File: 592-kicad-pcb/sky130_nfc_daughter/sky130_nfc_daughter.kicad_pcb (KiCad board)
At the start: 4 copper layers, 50 x 52 mm, 109 parts, among them J1 U.FL-R-SMT-1_80_, J10 U.FL-R-SMT-1_80_, J2 U.FL-R-SMT-1_80_, J3 U.FL-R-SMT-1_80_, J4 U.FL-R-SMT-1_80_, J5 U.FL-R-SMT-1_80_, J6 U.FL-R-SMT-1_80_, J7 U.FL-R-SMT-1_80_, J8 DF40C-40DS-0.4V_51_, J9 DF40C-40DS-0.4V_51_, SW1 SW_Push, U1 Caravel_QFN, U3 W25Q32JVZP

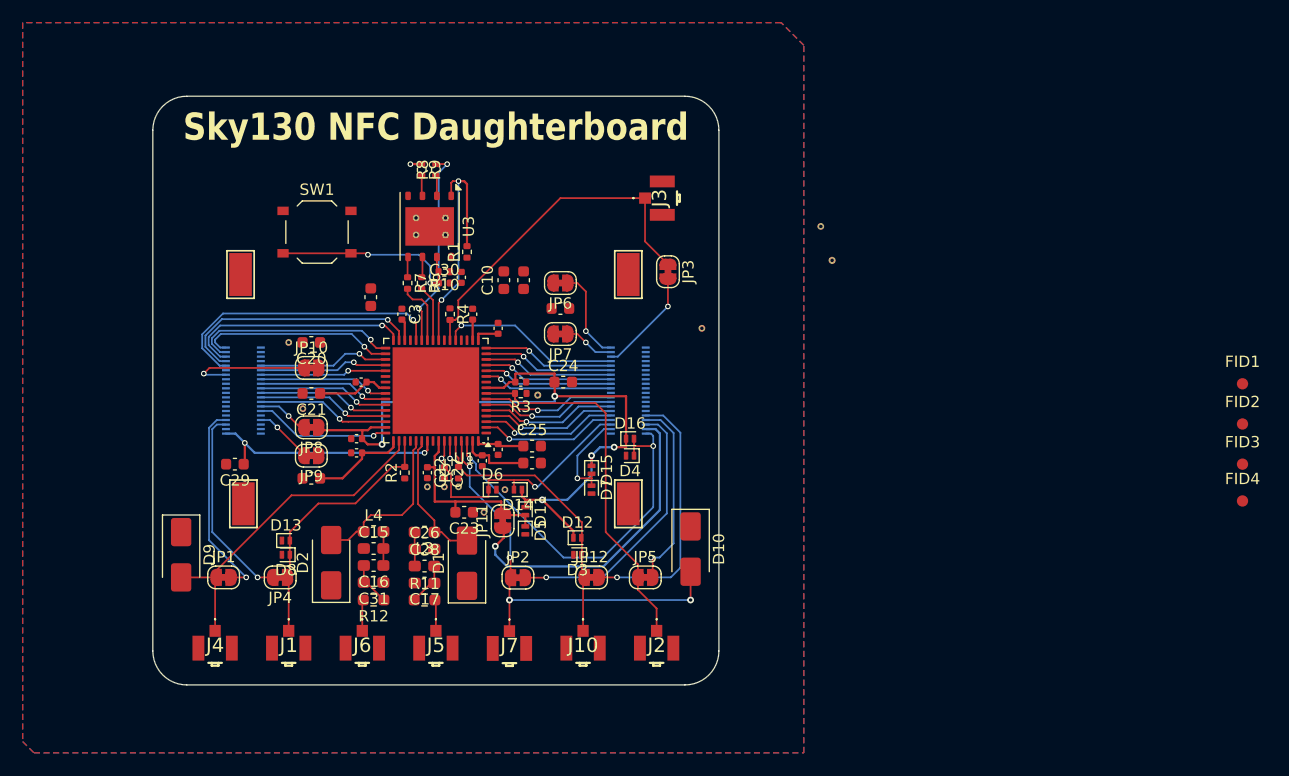
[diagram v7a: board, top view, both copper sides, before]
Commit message: daughterboard routing, 90% done
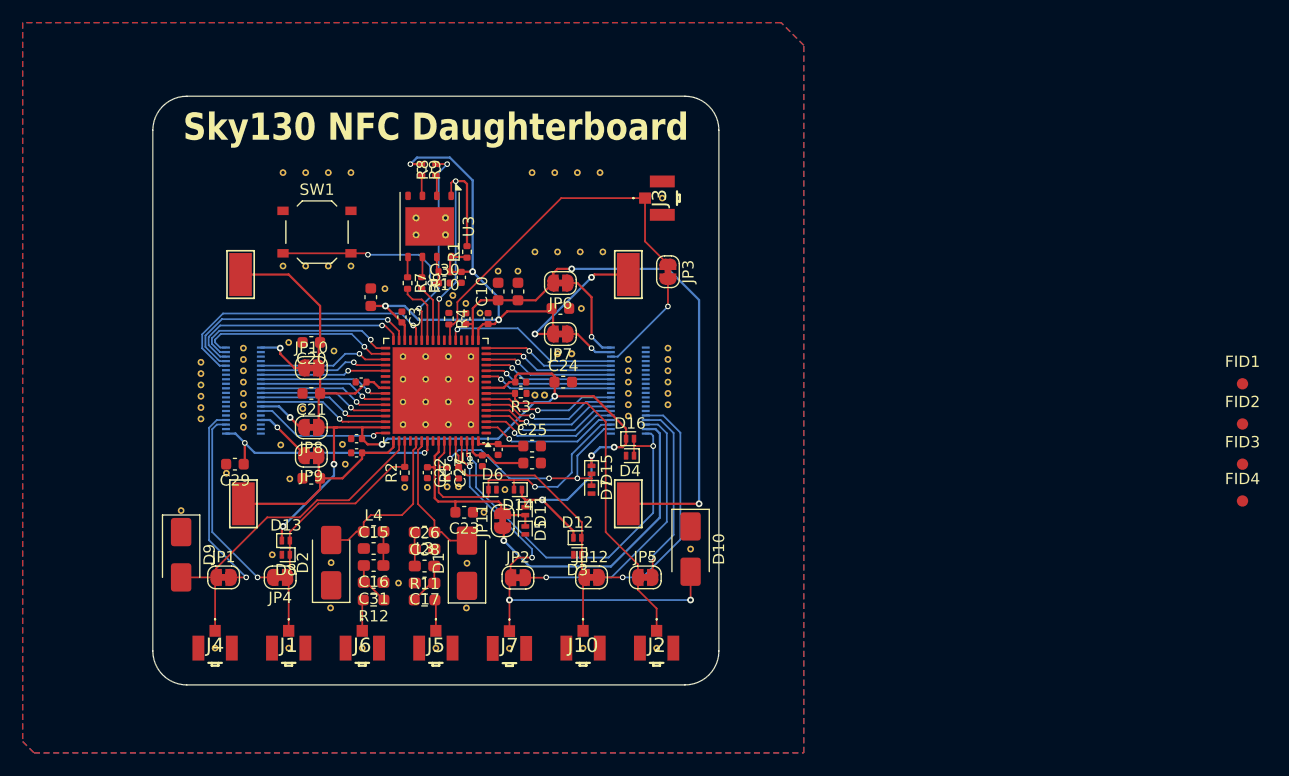
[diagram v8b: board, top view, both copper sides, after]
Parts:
- removed the REF** at (108.5, 31.5)
- removed the REF** at (98.0, 40.5)
- removed the STITCHM1 at (109.5, 34.5)
- added ?: , , F.Cu at (57.5, 45.2)
- added ?: , , F.Cu at (68.0, 68.8)
- added ?: , , F.Cu at (66.5, 52.5)
- added ?: , , F.Cu at (73.6, 49.0)
- added ?: , , F.Cu at (95.0, 47.2)
- added ?: , , F.Cu at (53.8, 43.5)
- added ?: , , F.Cu at (53.8, 45.5)
- added ?: , , F.Cu at (75.6, 45.0)
- added ?: , , F.Cu at (95.0, 44.2)
- added ?: , , F.Cu at (75.6, 47.0)
- added ?: , , F.Cu at (85.2, 33.8)
- added ?: , , F.Cu at (65.0, 26.8)
- added ?: , , F.Cu at (61.5, 68.8)
- added ?: , , F.Cu at (53.8, 46.5)
- added ?: , , F.Cu at (94.5, 29.0)
- added ?: , , F.Cu at (71.6, 43.0)
- added ?: , , F.Cu at (83.2, 33.8)
- added ?: , , F.Cu at (78.4, 39.1)
- added ?: , , F.Cu at (95.0, 45.2)
- added ?: , , F.Cu at (60.8, 50.8)
- added ?: , , F.Cu at (57.5, 46.2)
- added ?: , , F.Cu at (56.0, 53.3)
- added ?: , , F.Cu at (81.8, 35.5)
- added ?: , , F.Cu at (53.8, 47.5)
- added ?: , , F.Cu at (77.6, 45.0)
- added ?: , , F.Cu at (80.0, 35.5)
- added ?: , , F.Cu at (94.0, 68.8)
- added ?: , , F.Cu at (95.0, 42.2)
- added ?: , , F.Cu at (73.6, 47.0)
- added ?: , , F.Cu at (76.0, 37.6)
- added ?: , , F.Cu at (91.5, 45.2)
- added ?: , , F.Cu at (65.5, 42.5)
- added ?: , , F.Cu at (57.5, 48.2)
- added ?: , , F.Cu at (75.6, 49.0)
- added ?: , , F.Cu at (70.0, 37.0)
- added ?: , , F.Cu at (77.6, 43.0)
- added ?: , , F.Cu at (61.0, 26.8)
- added ?: , , F.Cu at (91.5, 46.2)
- added ?: , , F.Cu at (71.8, 54.5)
- added ?: , , F.Cu at (71.6, 47.0)
- added ?: , , F.Cu at (95.0, 43.2)
- added ?: , , F.Cu at (71.6, 45.0)
- added ?: , , F.Cu at (73.6, 45.0)
- added ?: , , F.Cu at (91.5, 43.2)
- added ?: , , F.Cu at (61.0, 35.0)
- added ?: , , F.Cu at (83.0, 26.8)
- added ?: , , F.Cu at (89.2, 33.8)
- added ?: , , F.Cu at (67.0, 26.8)
- added ?: , , F.Cu at (91.5, 44.2)
- added ?: , , F.Cu at (84.1, 46.4)
- added ?: , , F.Cu at (75.6, 43.0)
- added ?: , , F.Cu at (57.5, 49.2)
- added ?: , , F.Cu at (91.5, 47.2)
- added ?: , , F.Cu at (65.2, 65.2)
- added ?: , , F.Cu at (71.6, 49.0)
- added ?: , , F.Cu at (75.7, 38.3)
- added ?: , , F.Cu at (53.8, 48.5)
- added ?: , , F.Cu at (73.6, 43.0)
- added ?: , , F.Cu at (65.2, 61.2)
- added ?: , , F.Cu at (57.5, 43.2)
- added ?: , , F.Cu at (87.0, 26.8)
- added ?: , , F.Cu at (60.0, 60.5)
- added ?: , , F.Cu at (52.0, 56.6)
- added ?: , , F.Cu at (71.2, 63.0)
- added ?: , , F.Cu at (57.5, 42.2)
- added ?: , , F.Cu at (89.0, 26.8)
- added ?: , , F.Cu at (65.0, 35.0)
- added ?: , , F.Cu at (55.0, 68.8)
- added ?: , , F.Cu at (67.0, 35.0)
- added ?: , , F.Cu at (85.0, 26.8)
- added ?: , , F.Cu at (81.0, 68.8)
- added ?: , , F.Cu at (77.2, 38.3)
- added ?: , , F.Cu at (77.6, 49.0)
- added ?: , , F.Cu at (77.6, 47.0)
- added ?: , , F.Cu at (77.2, 65.2)
- added ?: , , F.Cu at (53.8, 44.5)
- added ?: , , F.Cu at (86.5, 42.8)
- added ?: , , F.Cu at (63.0, 26.8)
- added ?: , , F.Cu at (61.6, 53.8)
- added ?: , , F.Cu at (57.5, 44.2)
- added ?: , , F.Cu at (74.5, 68.8)
- added ?: , , F.Cu at (95.0, 46.2)
- added ?: , , F.Cu at (87.5, 68.8)
- added ?: , , F.Cu at (87.2, 33.8)
- added ?: , , F.Cu at (57.5, 47.2)
- added ?: , , F.Cu at (63.0, 35.0)
- added ?: , , F.Cu at (91.5, 48.2)
- added ?: , , F.Cu at (85.2, 42.8)
- added ?: , , F.Cu at (87.3, 38.8)
- added ?: , , F.Cu at (66.2, 50.8)
- added ?: , , F.Cu at (77.2, 61.2)
- added ?: , , F.Cu at (97.0, 60.0)
- moved C7 1.24 mm to (79.1, 39.6)
- moved C10 1.12 mm to (80.0, 37.2)
- moved C2 1.12 mm to (81.8, 37.2)
- moved C4 0.72 mm to (77.2, 39.6)
- moved R4 0.41 mm to (75.7, 39.6)
- moved C27 0.25 mm to (75.5, 53.2)
- moved C3 0.25 mm to (71.5, 39.5)
- moved REF** 0.25 mm to (75.5, 54.5)
- moved STITCHM1 0.25 mm to (83.2, 46.4)
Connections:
- J6 pad 3: unconnected-(J6-Pad3) -> GND
- J8 pad 1: GND -> /JA_vdda_user_3v3
- J8 pad 14: /JA_vdda_user_3v3 -> GND
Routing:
- net vddio_vdda_mgmt_3v3: track 9.89 -> 68.3 mm, vias 1 -> 6
- net vccd_mgmt_1v8: track 1.82 -> 50.7 mm, vias 0 -> 2
- net vdda_user_3v3: track 74.0 -> 100.2 mm, vias 5 -> 7
- net /RESET_EXT: track 9.78 -> 22.4 mm, vias 2 -> 3
- net vccd_user_1v8: track 14.7 -> 24.7 mm
- net /JA_vdda_user_3v3: track 11.1 -> 4.85 mm
- net /VREF_EXT: track 24.7 -> 27.0 mm, vias 2 -> 1
- net /ANA_MUX_OUT_2_EXT: track 37.3 -> 39.5 mm
- net /J_FS_EXT: track 23.2 -> 21.7 mm
- net /J_VDD_EXT: track 27.9 -> 26.5 mm
- net /NFC_AFE_TDO_EXT: track 33.9 -> 35.1 mm
